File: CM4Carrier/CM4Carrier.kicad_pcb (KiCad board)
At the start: 2 copper layers, 125 x 84 mm, 135 parts, among them J1 Micro_SD_Card, J2 Conn_01x04_Female, J3 USB_A, J4 USB_C_Receptacle_USB2.0, J5 1-84952-5, J6 AudioJack3_Dual_Ground_Switch, SW1 SW_Push, SW10 SW_Push, SW11 SW_Push, SW2 SW_Push, SW3 SW_Push, SW4 SW_Push, SW5 SW_Push, SW6 SW_Push, SW7 SW_Push, SW8 SW_Push, SW9 SW_Push, U1 MIC2025-2YMM, U2 MAX77751, U3 MAX17261xxTD, U4 MIC2877, U5 74HC00, U6 MCP3002

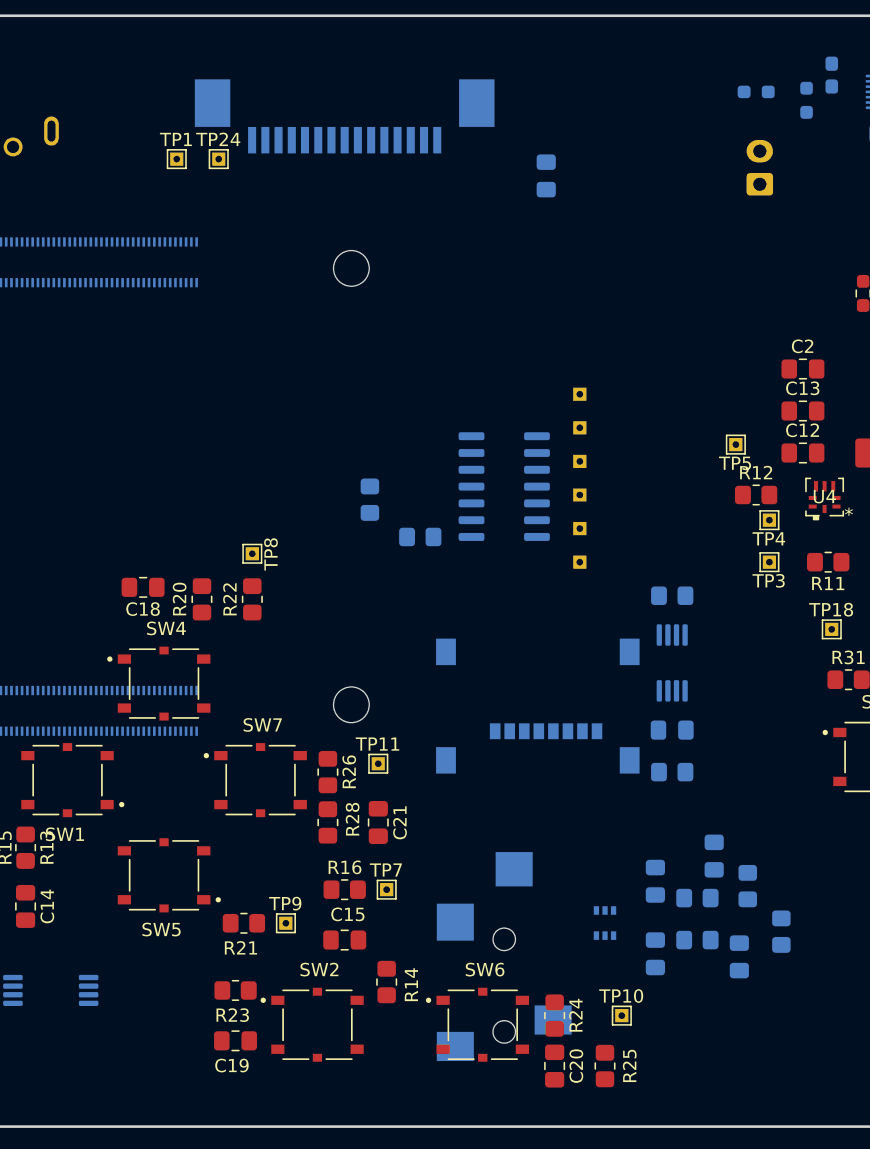
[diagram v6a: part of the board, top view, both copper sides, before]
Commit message: some fixes
cross reference with casing
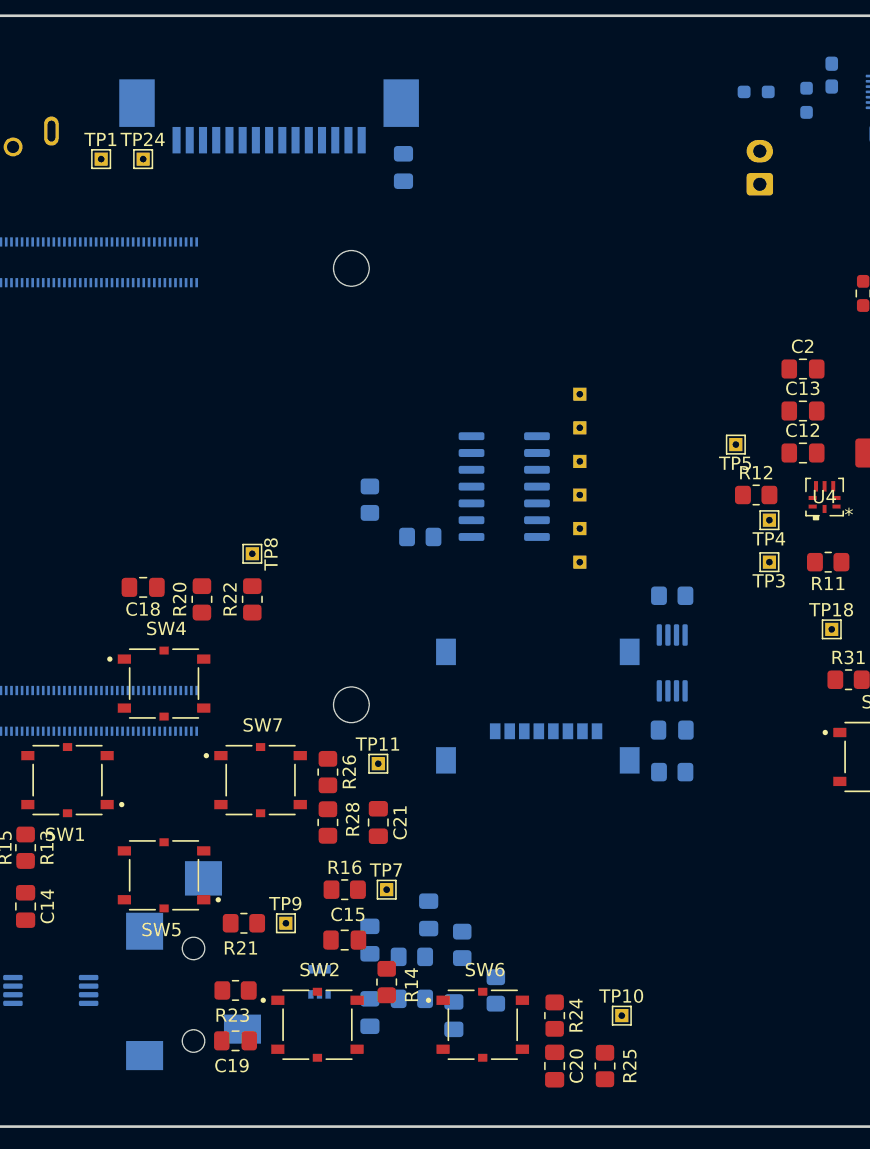
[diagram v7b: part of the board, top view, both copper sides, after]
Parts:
- moved J6 23.5 mm to (125.7, 131.5)
- moved C27 22.0 mm to (143.5, 124.5)
- moved C28 22.0 mm to (145.4, 132.1)
- moved C29 22.0 mm to (139.1, 126.4)
- moved C30 22.0 mm to (139.1, 131.8)
- moved D4 22.0 mm to (135.3, 129.5)
- moved R40 22.0 mm to (148.6, 130.2)
- moved R41 22.0 mm to (142.2, 127.6)
- moved R42 22.0 mm to (142.2, 130.8)
- moved R39 22.0 mm to (146.1, 126.7)
- moved C26 10.8 mm to (141.6, 67.9)
- moved J5 5.72 mm to (131.4, 65.9)
- moved TP24 5.72 mm to (121.9, 67.3)
- moved TP1 5.71 mm to (118.7, 67.3)
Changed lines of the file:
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@@
   )
   (footprint "TestPoint:TestPoint_THTPad_1.0x1.0mm_Drill0.5mm" (layer "F.Cu")
-    (at 124.46 67.31)
+    (at 118.745 67.31)
     (descr "THT rectangular pad as test Point, square 1.0mm side length, hole diameter 0.5mm")
     (tags "test point THT pad rectangle square")
@@
   )
   (footprint "TestPoint:TestPoint_THTPad_1.0x1.0mm_Drill0.5mm" (layer "F.Cu")
-    (at 127.635 67.31)
+    (at 121.92 67.31)
     (descr "THT rectangular pad as test Point, square 1.0mm side length, hole diameter 0.5mm")
     (tags "test point THT pad rectangle square")
@@
   )
   (footprint "Connector_Audio:Jack_3.5mm_CUI_SJ-3524-SMT_Horizontal" (layer "B.Cu")
-    (at 149.225 130.81)
+    (at 125.73 131.5)
     (descr "3.5 mm, Stereo, Right Angle, Surface Mount (SMT), Audio Jack Connector (https://www.cui.com/product/resource/sj-352x-smt-series.pdf)")
     (tags "3.5mm audio cui horizontal jack stereo")
@@
   )
   (footprint "Package_TO_SOT_SMD:SOT-363_SC-70-6" (layer "B.Cu")
-    (at 156.845 125.08 -90)
+    (at 135.255 129.525 -90)
     (descr "SOT-363, SC-70-6")
     (tags "SOT-363 SC-70-6")
@@
   )
   (footprint "Capacitor_SMD:C_0805_2012Metric_Pad1.18x1.45mm_HandSolder" (layer "B.Cu")
-    (at 152.4 68.58 -90)
+    (at 141.605 67.945 -90)
     (descr "Capacitor SMD 0805 (2012 Metric), square (rectangular) end terminal, IPC_7351 nominal with elongated pad for handsoldering. (Body size source: IPC-SM-782 page 76, https://www.pcb-3d.com/wordpress/wp-content/uploads/ipc-sm-782a_amendment_1_and_2.pdf, https://docs.google.com/spreadsheets/d/1BsfQQcO9C6DZCsRaXUlFlo91Tg2WpOkGARC1WS5S8t0/edit?usp=sharing), generated with kicad-footprint-generator")
     (tags "capacitor handsolder")
@@
   )
   (footprint "Capacitor_SMD:C_0805_2012Metric_Pad1.18x1.45mm_HandSolder" (layer "B.Cu")
-    (at 160.655 121.92 90)
+    (at 139.065 126.365 90)
     (descr "Capacitor SMD 0805 (2012 Metric), square (rectangular) end terminal, IPC_7351 nominal with elongated pad for handsoldering. (Body size source: IPC-SM-782 page 76, https://www.pcb-3d.com/wordpress/wp-content/uploads/ipc-sm-782a_amendment_1_and_2.pdf, https://docs.google.com/spreadsheets/d/1BsfQQcO9C6DZCsRaXUlFlo91Tg2WpOkGARC1WS5S8t0/edit?usp=sharing), generated with kicad-footprint-generator")
     (tags "capacitor handsolder")
@@
   )
   (footprint "Capacitor_SMD:C_0805_2012Metric_Pad1.18x1.45mm_HandSolder" (layer "B.Cu")
-    (at 160.655 127.4025 -90)
+    (at 139.065 131.8475 -90)
     (descr "Capacitor SMD 0805 (2012 Metric), square (rectangular) end terminal, IPC_7351 nominal with elongated pad for handsoldering. (Body size source: IPC-SM-782 page 76, https://www.pcb-3d.com/wordpress/wp-content/uploads/ipc-sm-782a_amendment_1_and_2.pdf, https://docs.google.com/spreadsheets/d/1BsfQQcO9C6DZCsRaXUlFlo91Tg2WpOkGARC1WS5S8t0/edit?usp=sharing), generated with kicad-footprint-generator")
     (tags "capacitor handsolder")
@@
   )
   (footprint "Resistor_SMD:R_0805_2012Metric_Pad1.20x1.40mm_HandSolder" (layer "B.Cu")
-    (at 167.64 122.285 90)
+    (at 146.05 126.73 90)
     (descr "Resistor SMD 0805 (2012 Metric), square (rectangular) end terminal, IPC_7351 nominal with elongated pad for handsoldering. (Body size source: IPC-SM-782 page 72, https://www.pcb-3d.com/wordpress/wp-content/uploads/ipc-sm-782a_amendment_1_and_2.pdf), generated with kicad-footprint-generator")
     (tags "resistor handsolder")
@@
   )
   (footprint "CM4IO:TE_1-84952-5" (layer "B.Cu")
-    (at 137.16 65.88)
+    (at 131.445 65.88)
     (property "Comment" "1-84952-5")
     (property "Sheetfile" "heiarchy/io_b.kicad_sch")
@@
   )
   (footprint "Resistor_SMD:R_0805_2012Metric_Pad1.20x1.40mm_HandSolder" (layer "B.Cu")
-    (at 170.18 125.73 90)
+    (at 148.59 130.175 90)
     (descr "Resistor SMD 0805 (2012 Metric), square (rectangular) end terminal, IPC_7351 nominal with elongated pad for handsoldering. (Body size source: IPC-SM-782 page 72, https://www.pcb-3d.com/wordpress/wp-content/uploads/ipc-sm-782a_amendment_1_and_2.pdf), generated with kicad-footprint-generator")
     (tags "resistor handsolder")
@@
   )
   (footprint "Resistor_SMD:R_0805_2012Metric_Pad1.20x1.40mm_HandSolder" (layer "B.Cu")
-    (at 163.83 126.365)
+    (at 142.24 130.81)
     (descr "Resistor SMD 0805 (2012 Metric), square (rectangular) end terminal, IPC_7351 nominal with elongated pad for handsoldering. (Body size source: IPC-SM-782 page 72, https://www.pcb-3d.com/wordpress/wp-content/uploads/ipc-sm-782a_amendment_1_and_2.pdf), generated with kicad-footprint-generator")
     (tags "resistor handsolder")
@@
   )
   (footprint "Capacitor_SMD:C_0805_2012Metric_Pad1.18x1.45mm_HandSolder" (layer "B.Cu")
-    (at 165.1 120.015 90)
+    (at 143.51 124.46 90)
     (descr "Capacitor SMD 0805 (2012 Metric), square (rectangular) end terminal, IPC_7351 nominal with elongated pad for handsoldering. (Body size source: IPC-SM-782 page 76, https://www.pcb-3d.com/wordpress/wp-content/uploads/ipc-sm-782a_amendment_1_and_2.pdf, https://docs.google.com/spreadsheets/d/1BsfQQcO9C6DZCsRaXUlFlo91Tg2WpOkGARC1WS5S8t0/edit?usp=sharing), generated with kicad-footprint-generator")
     (tags "capacitor handsolder")
@@
   )
   (footprint "Resistor_SMD:R_0805_2012Metric_Pad1.20x1.40mm_HandSolder" (layer "B.Cu")
-    (at 163.83 123.19)
+    (at 142.24 127.635)
     (descr "Resistor SMD 0805 (2012 Metric), square (rectangular) end terminal, IPC_7351 nominal with elongated pad for handsoldering. (Body size source: IPC-SM-782 page 72, https://www.pcb-3d.com/wordpress/wp-content/uploads/ipc-sm-782a_amendment_1_and_2.pdf), generated with kicad-footprint-generator")
     (tags "resistor handsolder")
@@
   )
   (footprint "Capacitor_SMD:C_0805_2012Metric_Pad1.18x1.45mm_HandSolder" (layer "B.Cu")
-    (at 167.005 127.635 -90)
+    (at 145.415 132.08 -90)
     (descr "Capacitor SMD 0805 (2012 Metric), square (rectangular) end terminal, IPC_7351 nominal with elongated pad for handsoldering. (Body size source: IPC-SM-782 page 76, https://www.pcb-3d.com/wordpress/wp-content/uploads/ipc-sm-782a_amendment_1_and_2.pdf, https://docs.google.com/spreadsheets/d/1BsfQQcO9C6DZCsRaXUlFlo91Tg2WpOkGARC1WS5S8t0/edit?usp=sharing), generated with kicad-footprint-generator")
     (tags "capacitor handsolder")

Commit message: fuseeeeeeeeeeeeeeeeeeeeeeeeeeeeeeeeeeeeeeeeeee
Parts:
- added F1: Polyfuse, Fuse:Fuse_1210_3225Metric_Pad1.42x2.65mm_HandSolder, B.Cu at (100.3, 69.8)
- added F2: Polyfuse, Fuse:Fuse_0805_2012Metric_Pad1.15x1.40mm_HandSolder, B.Cu at (193.0, 67.3)
- moved TP9 23.9 mm to (109.9, 118.1)
- moved TP6 23.4 mm to (104.8, 102.9)
- moved C19 22.2 mm to (109.9, 122.6), turned to -90 degrees
- moved C14 18.5 mm to (104.8, 107.3)
- moved R23 17.0 mm to (113.7, 122.6), turned to 90 degrees
- moved C22 13.6 mm to (170.8, 113.7)
- moved R21 13.0 mm to (116.8, 122.6), turned to 90 degrees
- moved R13 12.2 mm to (111.1, 107.3), turned to 90 degrees
- moved R15 12.2 mm to (108.0, 107.3), turned to 90 degrees
- moved R31 11.7 mm to (170.8, 117.5), turned to 180 degrees
- moved TP18 9.88 mm to (167.0, 109.9)
- moved R30 8.84 mm to (170.8, 109.9)
- moved C17 7.85 mm to (195.6, 87.6), turned to 90 degrees
- moved R29 7.65 mm to (142.9, 99.7), turned to -90 degrees
- moved R19 7.43 mm to (198.1, 95.0), turned to -90 degrees
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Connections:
- J3 pad 1: /_5v -> Net-(J3-Pad1)
- J4 pad A4/B9: /Battery/CHRG-VBUS -> Net-(J4-PadA4/B9)
- J4 pad B4/A9: /Battery/CHRG-VBUS -> Net-(J4-PadA4/B9)
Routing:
- net /_5v: track 0.00 -> 109.6 mm, vias 0 -> 6
- net /IO B/D+: track 0.00 -> 45.1 mm
- net /IO B/D-: track 0.00 -> 44.5 mm
- net /bi3: track 0.00 -> 39.7 mm
- net /bi7: track 0.00 -> 37.1 mm
- net /bi9: track 0.00 -> 32.9 mm
- net Net-(C16-Pad2): track 0.00 -> 31.8 mm
- net /bi2: track 0.00 -> 29.5 mm
- net /bi8: track 0.00 -> 28.4 mm
- net /bi6: track 0.00 -> 20.0 mm
- net /IO/SD_PWR: track 0.00 -> 19.8 mm
- net /bi4: track 0.00 -> 17.6 mm
- net Net-(J2-Pad4): track 0.00 -> 17.3 mm
- net /bi1: track 0.00 -> 12.5 mm
- net Net-(J2-Pad2): track 0.00 -> 11.7 mm, vias 0 -> 1
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- added copper zone on F.Cu, net GND
